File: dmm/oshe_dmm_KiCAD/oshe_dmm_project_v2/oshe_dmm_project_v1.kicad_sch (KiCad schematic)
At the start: 69 parts, among them J1 FTDI Basic, J10 Voltage Range 2, J11 Voltage Range 3, J12 Voltage Range 3, J13 Current Indication, J2 Voltage, J3 GND, J4 Current, J6 ON/OFF, J7 Voltage Range 1, J8 Voltage Range 1, J9 Voltage Range 2, SW1 PTS526 SK15 SMTR2 LFS, U1 ATmega328P-A, U2 INA219BxD, U3 ADS1115IDGS, U5 LM317_SOT-223, Y1 16MHz

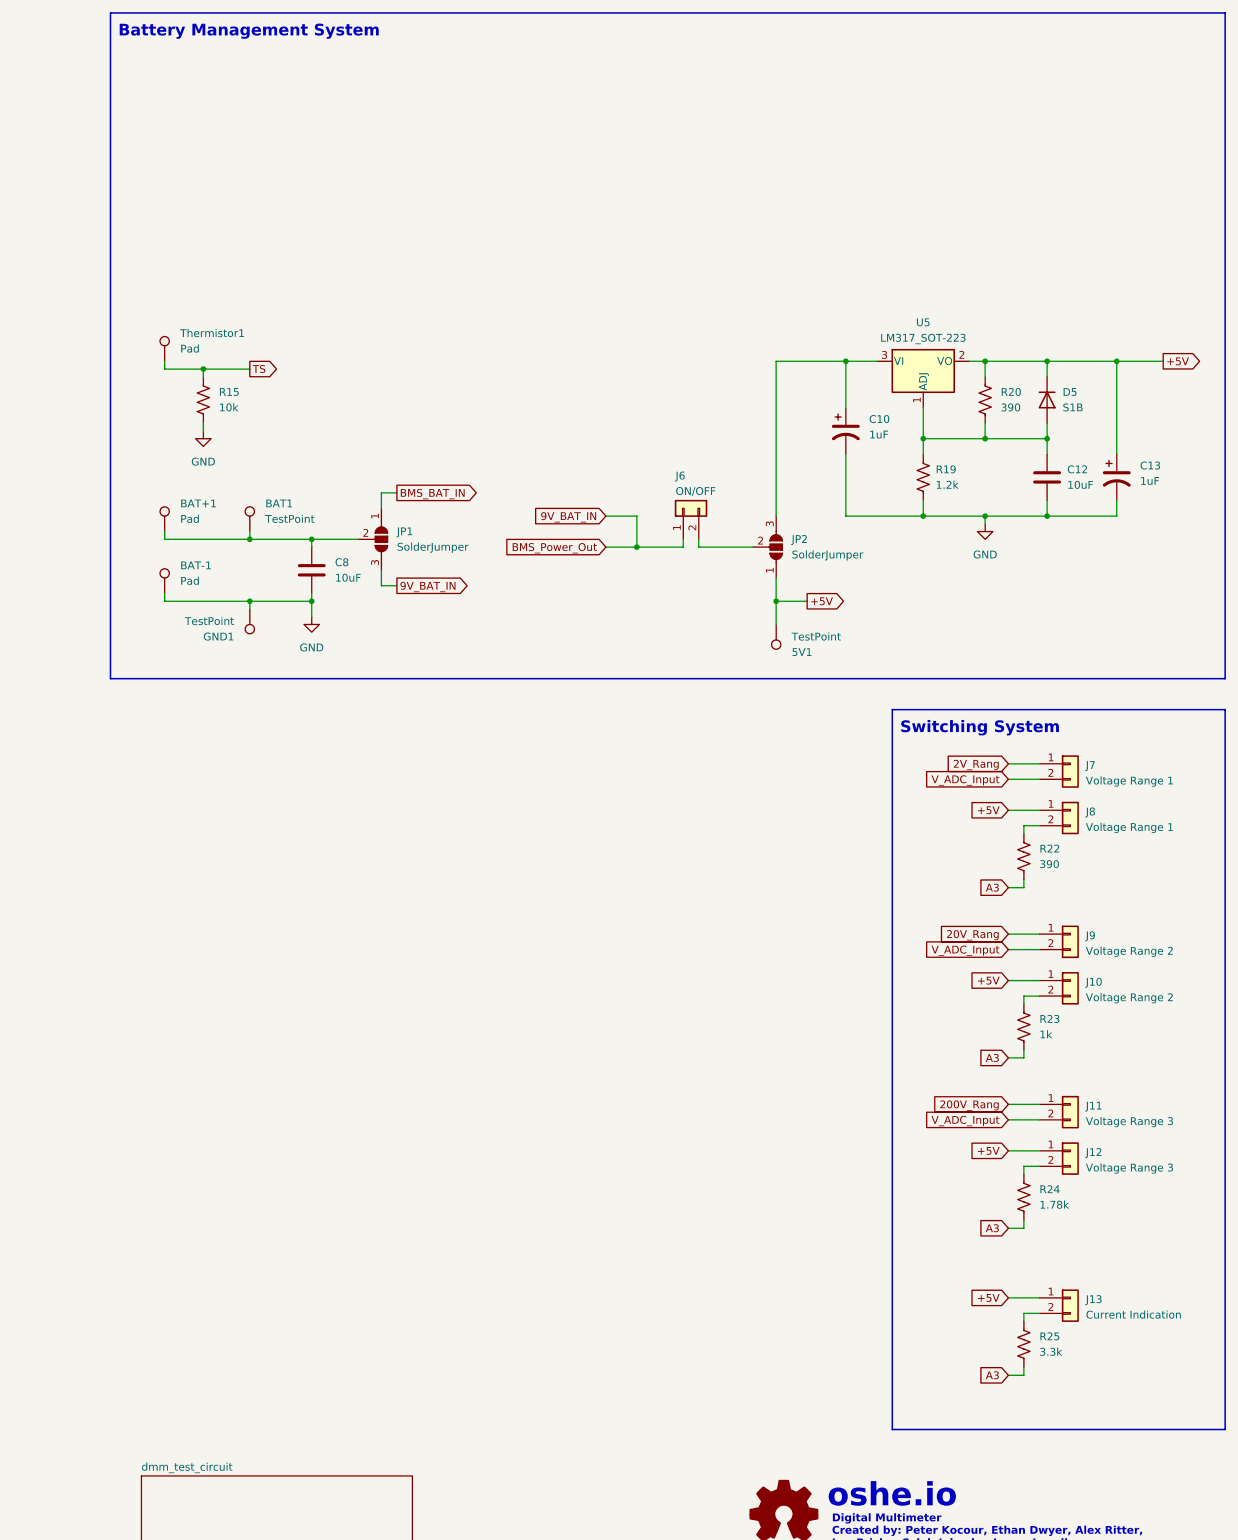
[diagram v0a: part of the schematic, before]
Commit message: schematic of res meas
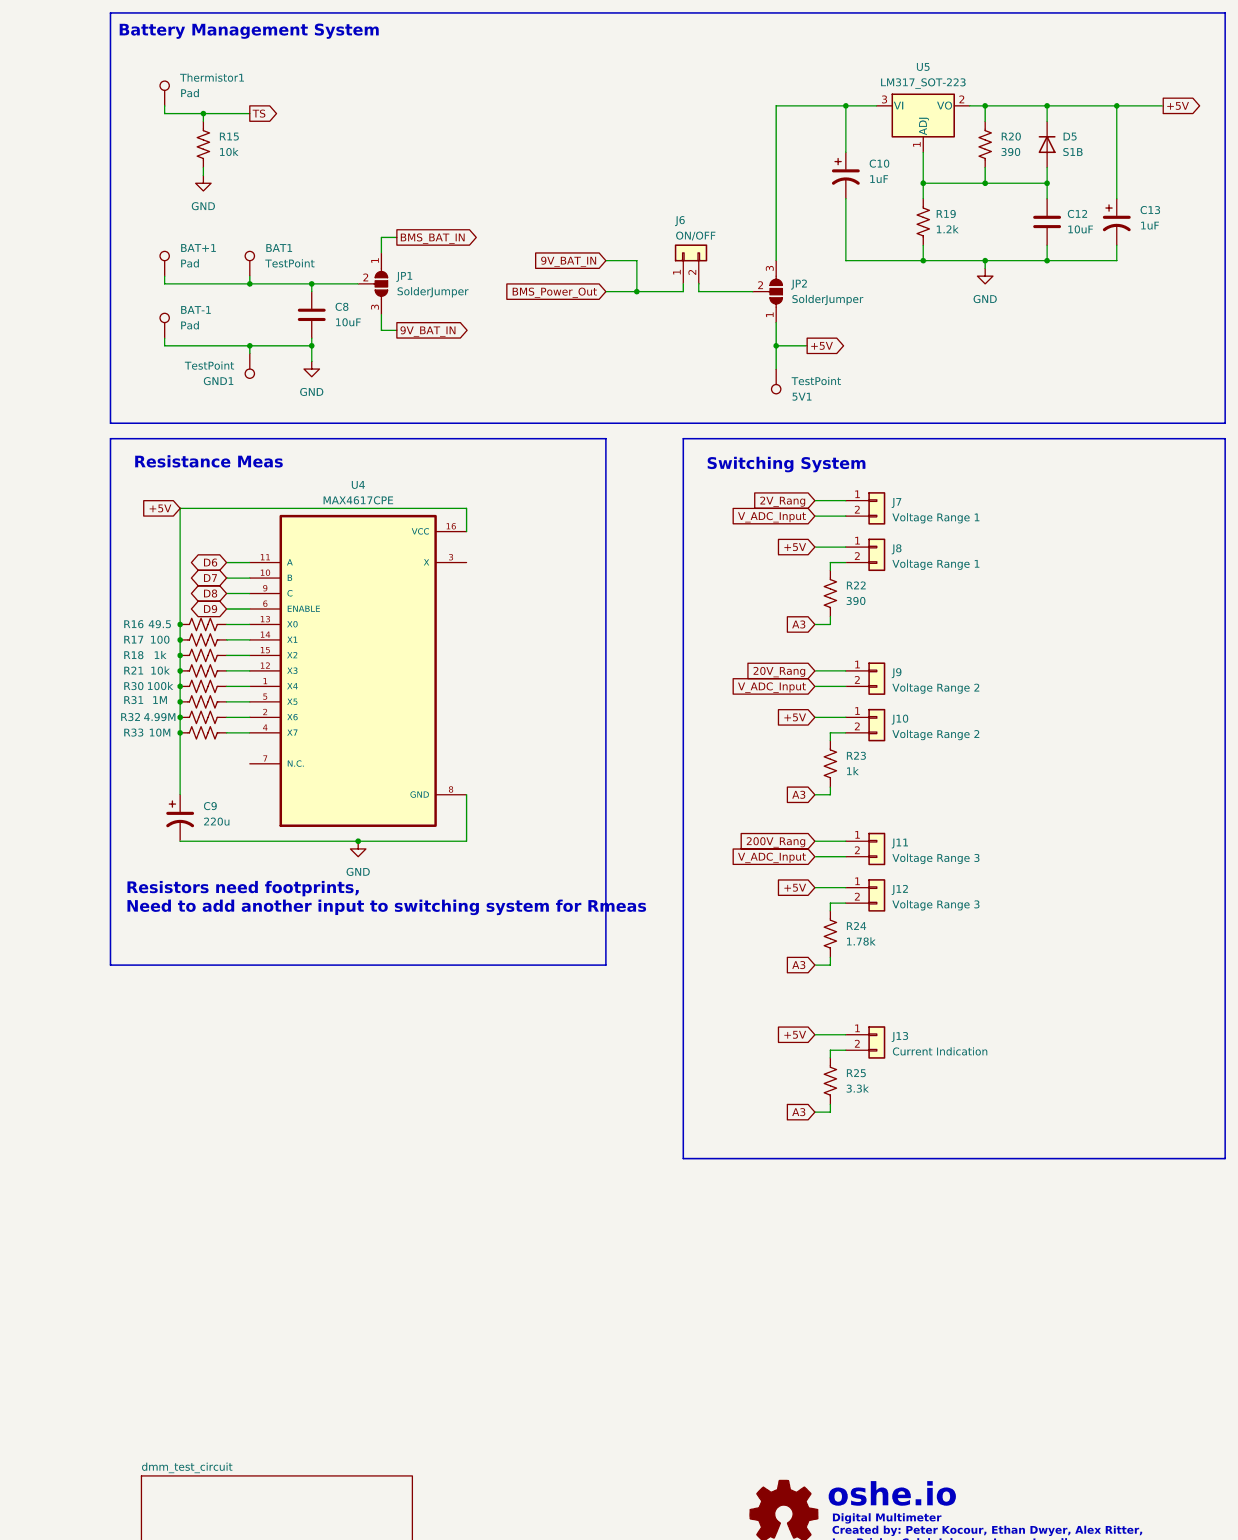
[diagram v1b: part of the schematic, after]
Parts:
- added C9: 220u, symbol Device:C_Polarized_US
- added R16: 49.5, symbol Device:R_US
- added R17: 100, symbol Device:R_US
- added R18: 1k, symbol Device:R_US
- added R21: 10k, symbol Device:R_US
- added R30: 100k, symbol Device:R_US
- added R31: 1M, symbol Device:R_US
- added R32: 4.99M, symbol Device:R_US
- added R33: 10M, symbol Device:R_US
- added U4: MAX4617CPE, DIP794W47P254L1943H457Q16, symbol MAX4617CPE:MAX4617CPE
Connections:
- net +5V: now also C9.1, R16.1, R17.1, R18.1, R21.1, R30.1, R31.1, R32.1, R33.1, U4.16 (VCC)
- net D6: now also U4.11 (A)
- net D7: now also U4.10 (B)
- net D8: now also U4.9 (C)
- net D9: now also U4.6 (ENABLE)
- net GND: now also C9.2, U4.8 (GND)
- new net: R30.2, U4.1 (X4)
- new net: R21.2, U4.12 (X3)
- new net: R16.2, U4.13 (X0)
- new net: R17.2, U4.14 (X1)
- new net: R18.2, U4.15 (X2)
- new net: R32.2, U4.2 (X6)
- new net: R33.2, U4.4 (X7)
- new net: R31.2, U4.5 (X5)
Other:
- note added: "Resistance Meas"
- note added: "Resistors need footprints, Need to add another input to switching system for Rmeas"
- moved on the sheet: 5V1, BAT+1, BAT-1, BAT1, C10, C12, C13, C8, D5, GND1, J10, J11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

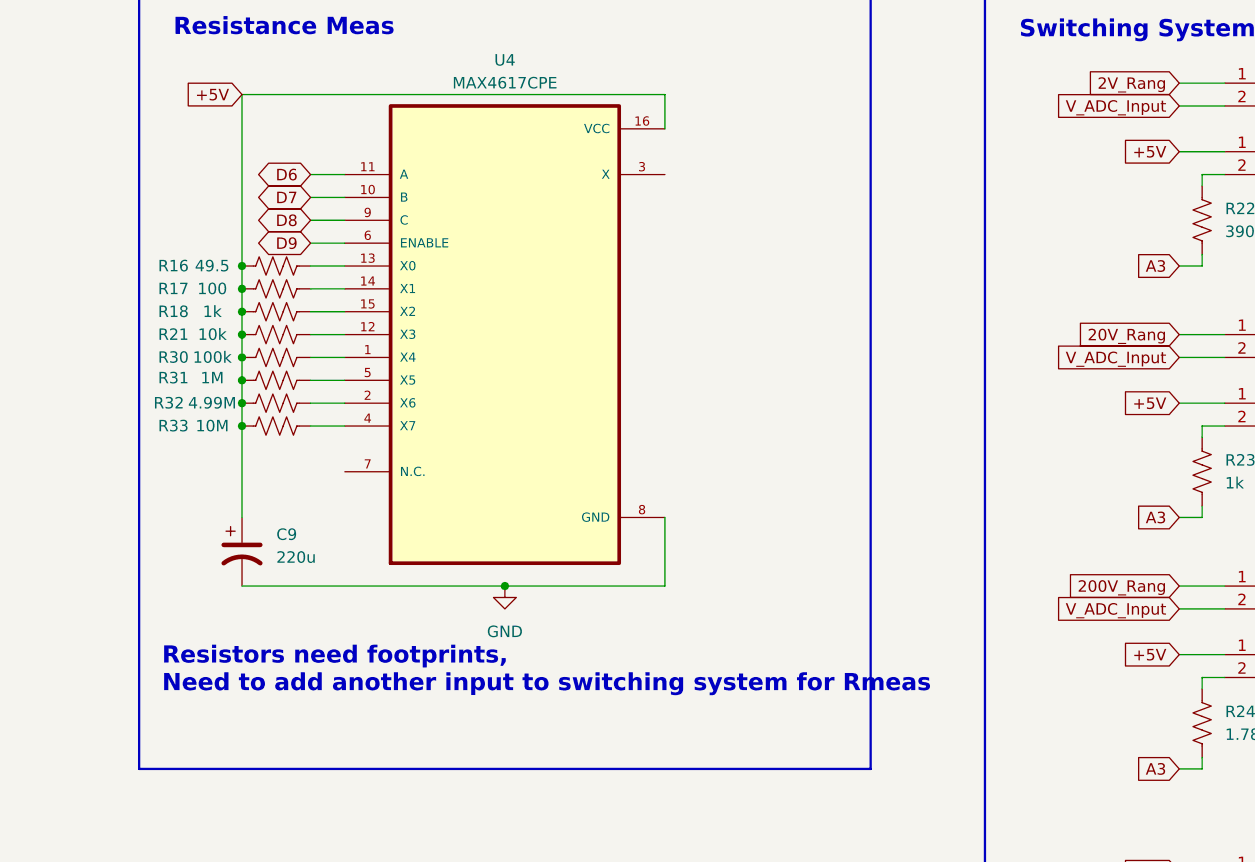
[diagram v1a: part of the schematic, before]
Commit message: Add res to pcb
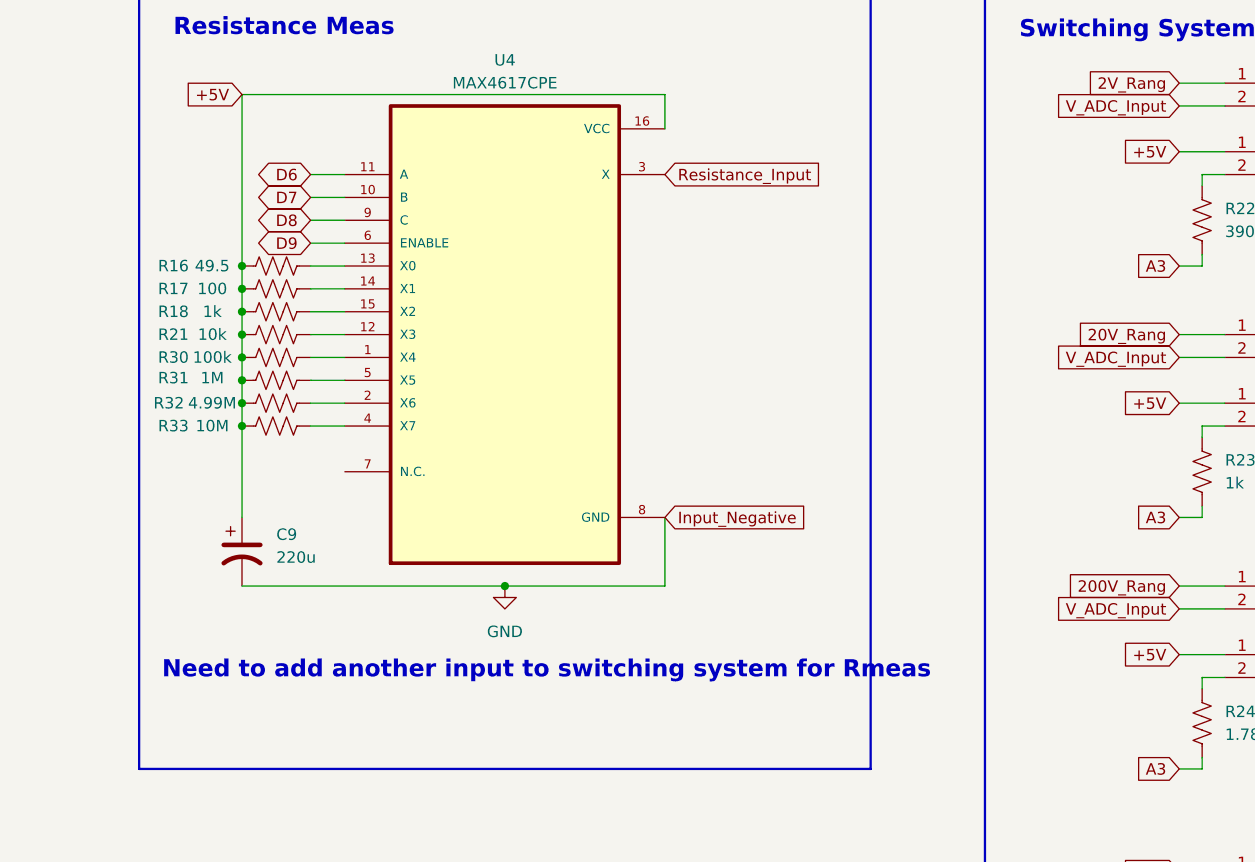
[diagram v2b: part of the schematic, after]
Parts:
- C9: footprint (none) -> Connector_PinHeader_2.54mm:PinHeader_1x02_P2.54mm_Vertical
- R16, R17, R18, R21, R30, R31, R32, R33: footprint (none) -> Resistor_SMD:R_1206_3216Metric_Pad1.30x1.75mm_HandSolder
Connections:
- net Input_Negative is gone; now on net GND: D1.2 (A2), D2.1 (A1), J3.1, R1.2, R7.2, U2.7 (IN-), U3.5 (AIN1)
- net Resistance_Input: now reaches U4.3 (X)
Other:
- note added: "Need to add another input to switching system for Rmeas"
- note removed: "Resistors need footprints, Need to add another input to switching system for Rmeas"
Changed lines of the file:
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@@
 		)
 	)
-	(text "Resistors need footprints, \nNeed to add another input to switching system for Rmeas"
+	(text "Need to add another input to switching system for Rmeas"
 		(exclude_from_sim no)
 		(at 223.52 160.528 0)
@@
 		)
 	)
+	(global_label "Input_Negative"
+		(shape input)
+		(at 279.4 143.51 0)
+		(fields_autoplaced yes)
+		(effects
+			(font
+				(size 1.27 1.27)
+			)
+			(justify left)
+		)
+		(property "Intersheetrefs" "${INTERSHEET_REFS}"
+			(at 262.5659 143.51 0)
+			(effects
+				(font
+					(size 1.27 1.27)
+				)
+				(justify right)
+				(hide yes)
+			)
+		)
+	)
 	(global_label "A3"
 		(shape input)
@@
 		)
 	)
+	(global_label "Resistance_Input"
+		(shape input)
+		(at 279.4 105.41 0)
+		(fields_autoplaced yes)
+		(effects
+			(font
+				(size 1.27 1.27)
+			)
+			(justify left)
+		)
+		(property "Intersheetrefs" "${INTERSHEET_REFS}"
+			(at 262.5659 105.41 0)
+			(effects
+				(font
+					(size 1.27 1.27)
+				)
+				(justify right)
+				(hide yes)
+			)
+		)
+	)
 	(symbol
 		(lib_id "Jumper:SolderJumper_3_Open")
@@
 			)
 		)
-		(property "Footprint" ""
+		(property "Footprint" "Resistor_SMD:R_1206_3216Metric_Pad1.30x1.75mm_HandSolder"
 			(at 236.474 122.174 90)
 			(effects
@@
 			)
 		)
-		(property "Footprint" ""
+		(property "Footprint" "Resistor_SMD:R_1206_3216Metric_Pad1.30x1.75mm_HandSolder"
 			(at 236.474 127.254 90)
 			(effects
@@
 			)
 		)
-		(property "Footprint" ""
+		(property "Footprint" "Resistor_SMD:R_1206_3216Metric_Pad1.30x1.75mm_HandSolder"
 			(at 236.474 129.794 90)
 			(effects
@@
 			)
 		)
-		(property "Footprint" ""
+		(property "Footprint" "Resistor_SMD:R_1206_3216Metric_Pad1.30x1.75mm_HandSolder"
 			(at 236.474 124.714 90)
 			(effects
@@
 			)
 		)
-		(property "Footprint" ""
+		(property "Footprint" "Resistor_SMD:R_1206_3216Metric_Pad1.30x1.75mm_HandSolder"
 			(at 236.474 114.554 90)
 			(effects
@@
 			)
 		)
-		(property "Footprint" ""
+		(property "Footprint" "Connector_PinHeader_2.54mm:PinHeader_1x02_P2.54mm_Vertical"
 			(at 232.41 147.32 0)
 			(effects
@@
 			)
 		)
-		(property "Footprint" ""
+		(property "Footprint" "Resistor_SMD:R_1206_3216Metric_Pad1.30x1.75mm_HandSolder"
 			(at 236.474 117.094 90)
 			(effects
@@
 			)
 		)
-		(property "Footprint" ""
+		(property "Footprint" "Resistor_SMD:R_1206_3216Metric_Pad1.30x1.75mm_HandSolder"
 			(at 236.474 119.634 90)
 			(effects
@@
 			)
 		)
-		(property "Footprint" ""
+		(property "Footprint" "Resistor_SMD:R_1206_3216Metric_Pad1.30x1.75mm_HandSolder"
 			(at 236.474 132.334 90)
 			(effects

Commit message: finished Resistance
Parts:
- added D4: SMAJ200A, Diode_SMD:D_SMA, symbol Diode:SMAJ200A
- added J5: Resistance Meas, Connector_PinHeader_2.54mm:PinHeader_1x02_P2.54mm_Vertical, symbol Connector_Generic:Conn_01x02
- added R34, R35: R?, Resistor_SMD:R_1206_3216Metric_Pad1.30x1.75mm_HandSolder, symbol Device:R_US
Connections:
- net Resistance_Input is gone; now on net A0: U4.3 (X)
- net +5V: now also J5.1 (Pin_1)
- net 2V_Rang: now also D4.1 (A1)
- net A0: now also D4.2 (A2)
- net A3: now also R34.1
- new net: J5.2 (Pin_2), R34.2
- no-connect marks 6 -> 8
